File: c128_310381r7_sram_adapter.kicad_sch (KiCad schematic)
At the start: 20 parts, among them J1 T_0_L_DRAM, J10 T_6_L_DRAM, J2 L_0_L_DRAM, J3 T_7_R_DRAM, J4 L_7_R_DRAM, J5 T_1_L_DRAM, J6 T_2_L_DRAM, J7 T_3_L_DRAM, J8 T_4_L_DRAM, J9 T_5_L_DRAM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

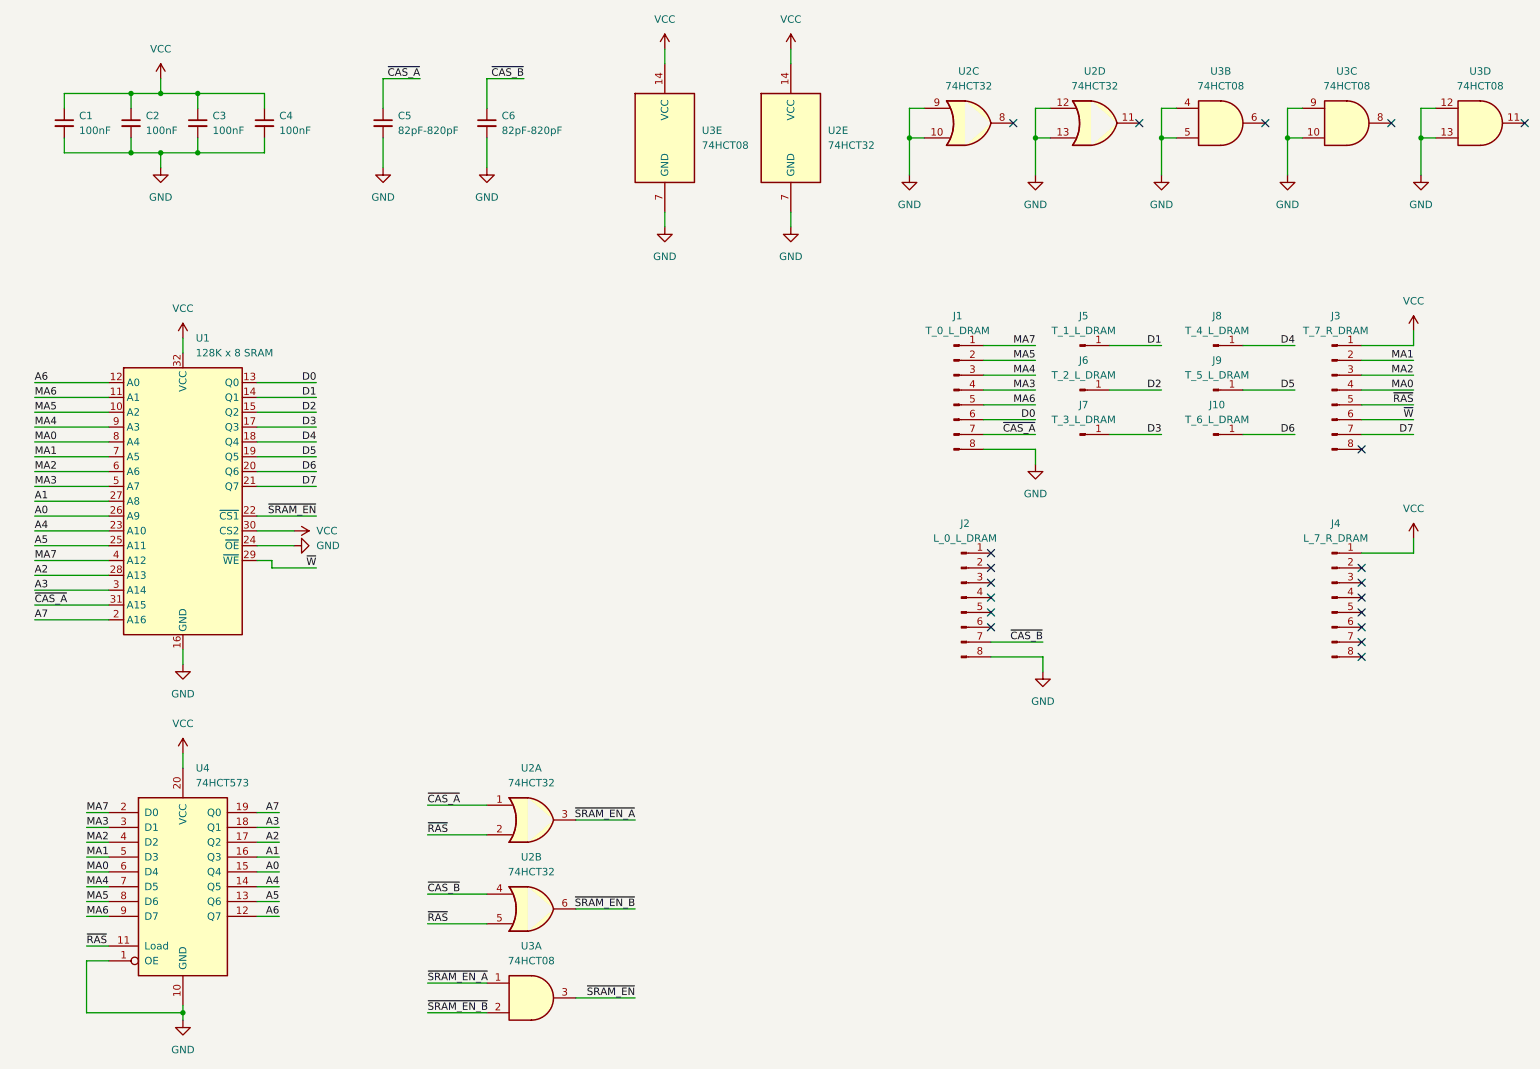
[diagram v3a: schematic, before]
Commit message: Begin drawing traces
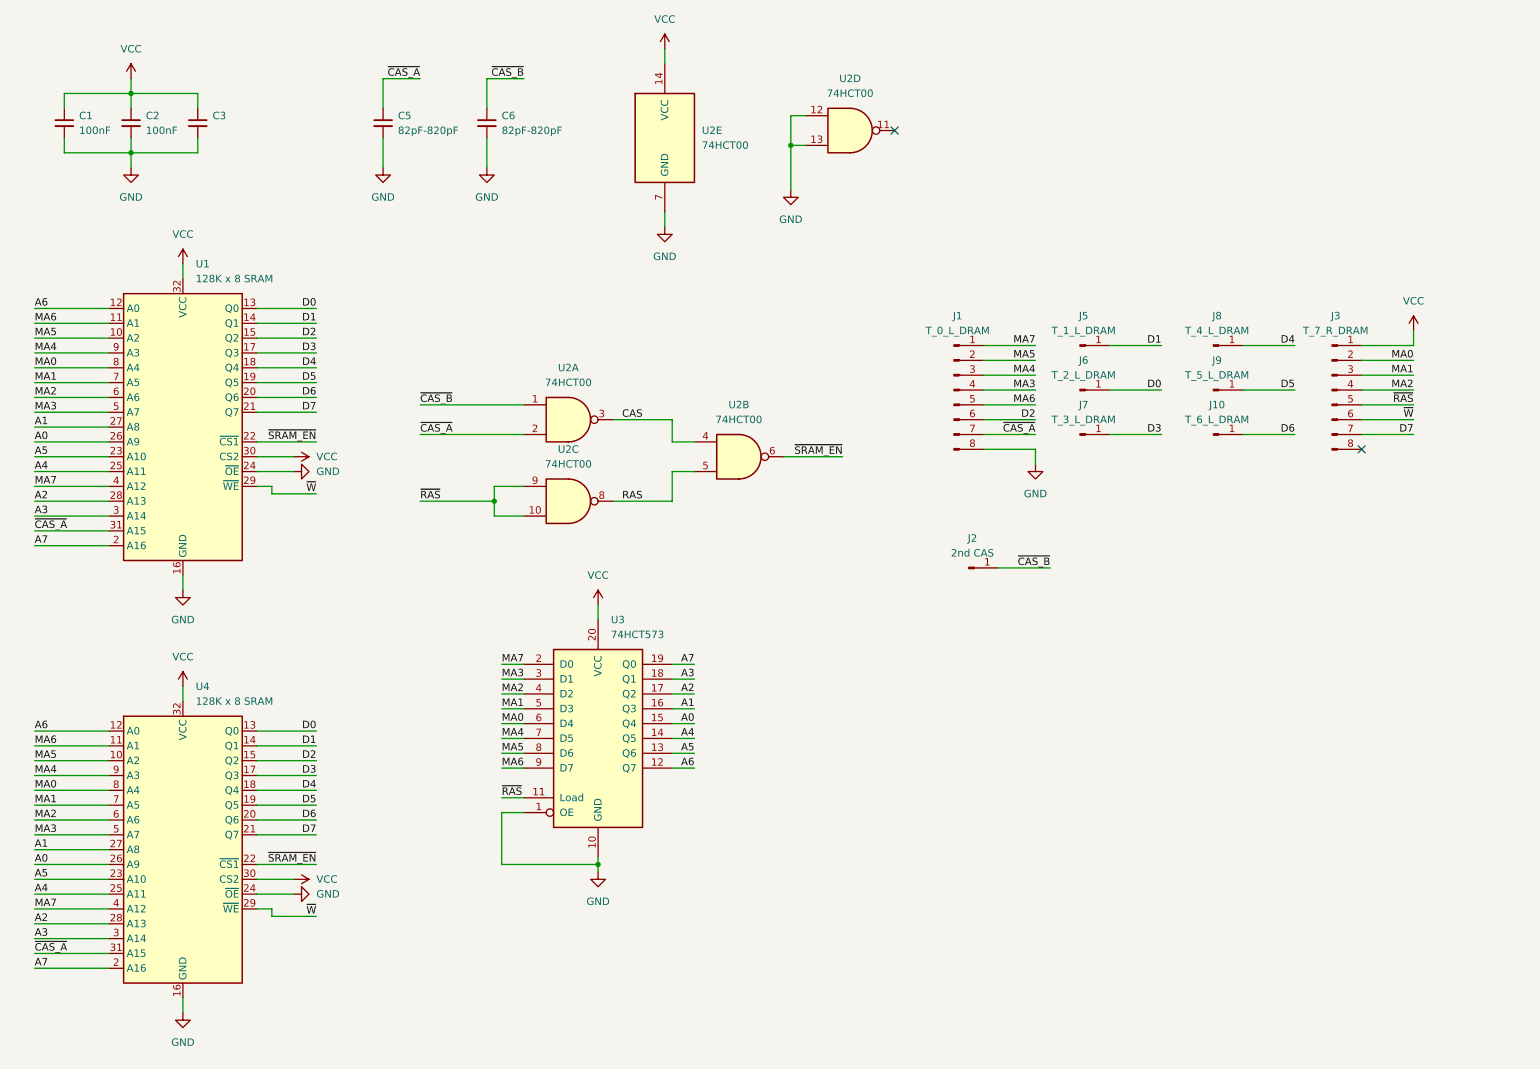
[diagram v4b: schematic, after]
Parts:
- removed C4: 100nF, DoubleFootprint_Library:C_Disc_1206_P5.00mm, symbol Device:C_Small
- removed J2: L_0_L_DRAM, Connector_PinHeader_2.54mm:PinHeader_1x08_P2.54mm_Vertical, symbol Connector:Conn_01x08_Pin
- removed J4: L_7_R_DRAM, Connector_PinHeader_2.54mm:PinHeader_1x08_P2.54mm_Vertical, symbol Connector:Conn_01x08_Pin
- removed U2: 74HCT32, DoubleFootprint_Library:DIP-SO-14, symbol 74xx:74LS32
- removed U3: 74HCT08, DoubleFootprint_Library:DIP-SO-14, symbol 74xx:74LS08
- added J2: 2nd CAS, Connector_PinHeader_2.54mm:PinHeader_1x01_P2.54mm_Horizontal, symbol Connector:Conn_01x01_Pin
- added U2: 74HCT00, DoubleFootprint_Library:DIP-SO-14, symbol 74xx:74LS00
- added U4: 128K x 8 SRAM, Package_SO:SOP-32_11.305x20.495mm_P1.27mm, symbol Memory_RAM:628128_DIP32_SSOP32
- U1: footprint DoubleFootprint_Library:DIP-SOP-32 -> Package_DIP:DIP-32_W15.24mm
- renumbered U4 to U3
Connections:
- net A0: now also U4.26 (A9)
- net A1: now also U4.27 (A8)
- net A2: now also U4.28 (A13)
- net A3: now also U4.3 (A14)
- net A4: now also U1.25 (A11), U4.25 (A11); no longer U1.23 (A10)
- net A5: now also U1.23 (A10), U4.23 (A10); no longer U1.25 (A11)
- net A6: now also U4.12 (A0)
- net A7: now also U4.2 (A16)
- net D0: now also J6.1 (Pin_1), U4.13 (Q0); no longer J1.6 (Pin_6)
- net D1: now also U4.14 (Q1)
- net D2: now also J1.6 (Pin_6), U4.15 (Q2); no longer J6.1 (Pin_1)
- net D3: now also U4.17 (Q3)
- net D4: now also U4.18 (Q4)
- net D5: now also U4.19 (Q5)
- net D6: now also U4.20 (Q6)
- net D7: now also U4.21 (Q7)
- net GND: now also U2.12, U2.13, U2.7 (GND), U4.16 (GND), U4.24 (~{OE})
- net MA0: now also J3.2 (Pin_2), U4.8 (A4); no longer J3.4 (Pin_4)
- net MA1: now also J3.3 (Pin_3), U4.7 (A5); no longer J3.2 (Pin_2)
- net MA2: now also J3.4 (Pin_4), U4.6 (A6); no longer J3.3 (Pin_3)
- net MA3: now also U4.5 (A7)
- net MA4: now also U4.9 (A3)
- net MA5: now also U4.10 (A2)
- net MA6: now also U4.11 (A1)
- net MA7: now also U4.4 (A12)
- net VCC: now also U2.14 (VCC), U4.30 (CS2), U4.32 (VCC)
- net ~{CAS_A}: now also U2.2, U4.31 (A15)
- net ~{CAS_B}: now also J2.1 (Pin_1), U2.1
- net ~{RAS}: now also U2.10, U2.9
- net ~{SRAM_EN}: now also U2.6, U4.22 (~{CS1})
- net ~{W}: now also U4.29 (~{WE})
- new net CAS: U2.3, U2.4
- new net RAS: U2.5, U2.8
- no-connect marks 19 -> 2
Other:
- moved on the sheet: U1, U3

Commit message: Complete routing of first revision of the adapter
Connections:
- net A6: now also U1.10 (A2), U4.10 (A2); no longer U1.12 (A0), U4.12 (A0)
- net MA5: now also U1.11 (A1), U4.11 (A1); no longer U1.10 (A2), U4.10 (A2)
- net MA6: now also U1.12 (A0), U4.12 (A0); no longer U1.11 (A1), U4.11 (A1)
- net ~{CAS_A}: no longer U1.31 (A15), U4.31 (A15)
- net ~{CAS_B}: now also U1.31 (A15), U4.31 (A15)
